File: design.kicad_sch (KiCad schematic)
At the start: 28 parts, among them J2 SKEDD:490107670612, U1 MCP1700x-330xxTT, U2 TCK108AF,LF, U3 ESP32-C3-WROOM-02-N4, U4 TTP223

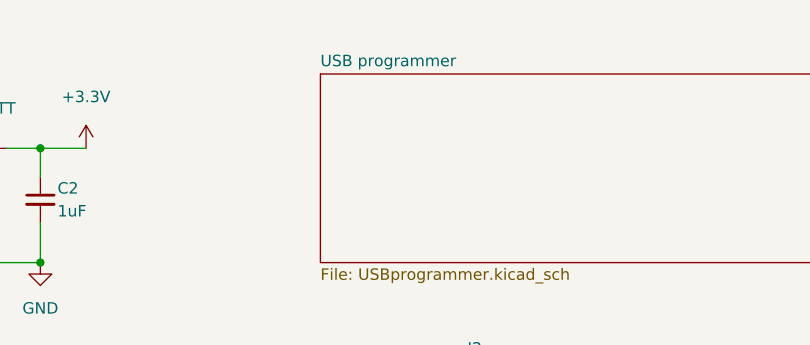
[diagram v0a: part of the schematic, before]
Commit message: remove " " in name
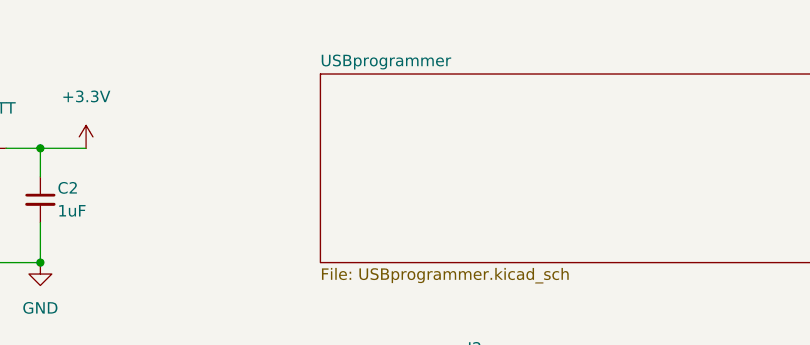
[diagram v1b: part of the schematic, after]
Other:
- sheet USB programmer renamed USBprogrammer
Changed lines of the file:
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@@
     (stroke (width 0.1524) (type solid) (color 0 0 0 0))
     (fill (color 0 0 0 0.0000))
-    (property "Sheet name" "USB programmer" (id 0) (at 207.645 20.8784 0)
+    (property "Sheet name" "USBprogrammer" (id 0) (at 207.645 20.8784 0)
       (effects (font (size 1.27 1.27)) (justify left bottom))
     )

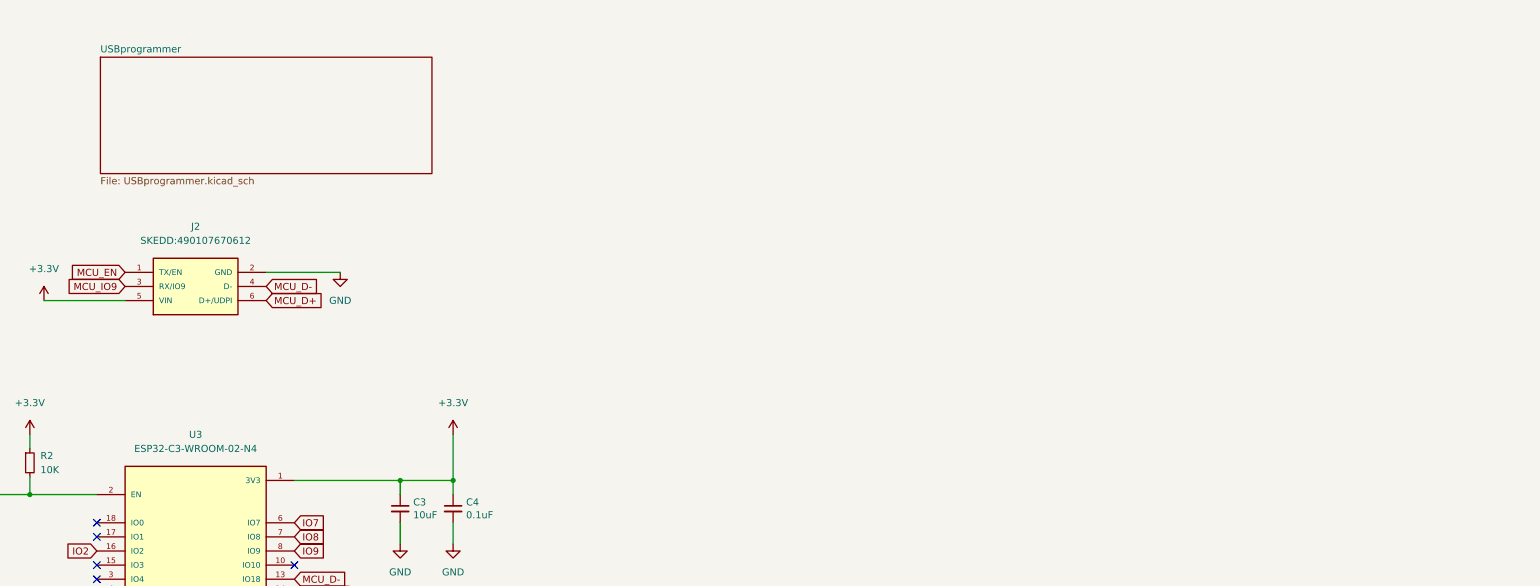
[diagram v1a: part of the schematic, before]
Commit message: revert subsheet in SCH
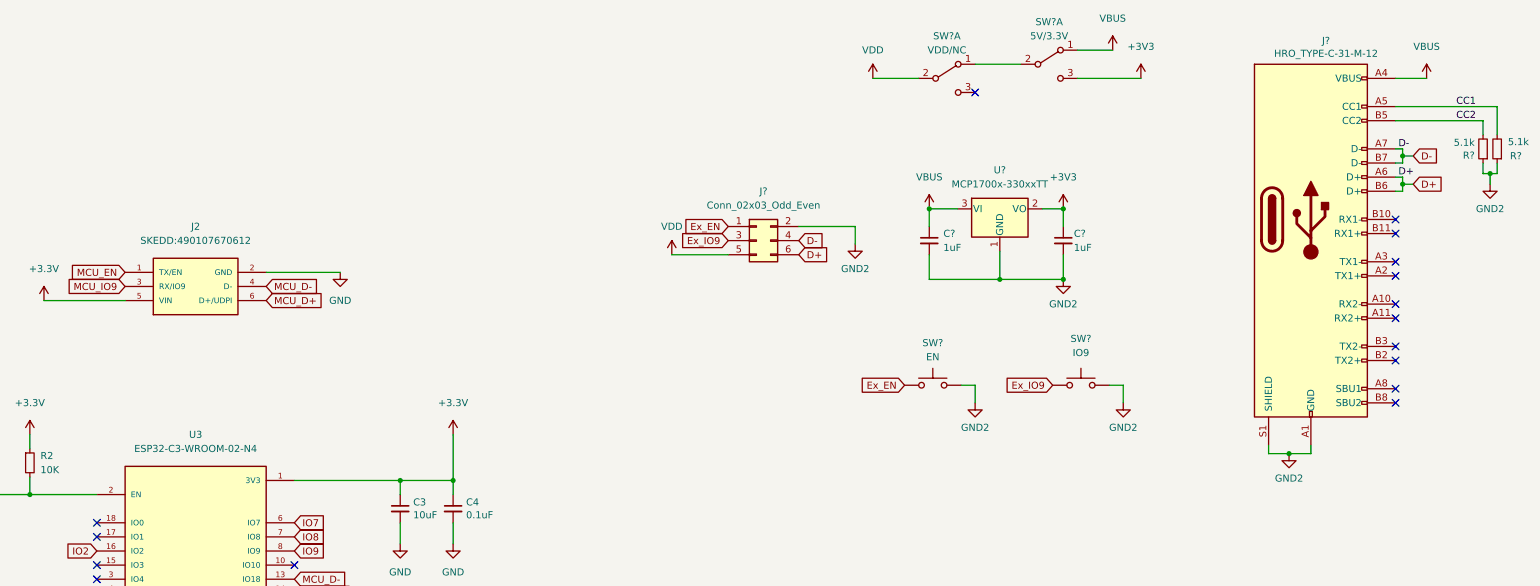
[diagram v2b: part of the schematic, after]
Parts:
- added C? (x2): 1uF, Capacitor_SMD:C_0805_2012Metric, symbol Device:C_Small
- added J?: Conn_02x03_Odd_Even, Connector_PinHeader_2.54mm:PinHeader_2x03_P2.54mm_Vertical, symbol Connector_Generic:Conn_02x03_Odd_Even
- added J?: HRO_TYPE-C-31-M-12, Connector_USB:USB_C_Receptacle_HRO_TYPE-C-31-M-12, symbol Connector:USB_C_Receptacle
- added R? (x2): 5.1k, Resistor_SMD:R_0805_2012Metric, symbol Device:R_Small
- added SW?: EN, Button_Switch_SMD_custom:RKB2, symbol Switch:SW_Push
- added SW?: IO9, Button_Switch_SMD_custom:RKB2, symbol Switch:SW_Push
- added SW?: VDD/NC, Button_Switch_SMD:SW_DPDT_CK_JS202011JCQN, symbol Switch:SW_DPDT_x2
- added SW?: 5V/3.3V, Button_Switch_SMD:SW_DPDT_CK_JS202011JCQN, symbol Switch:SW_DPDT_x2
- added U?: MCP1700x-330xxTT, Package_TO_SOT_SMD:SOT-23, symbol Regulator_Linear:MCP1700x-330xxTT
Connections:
- new net: SW?.1 (A), SW?.2 (B)
- new net +3V3: C?.1, SW?.3 (C), U?.2 (VO)
- new net CC1: J?.A5 (CC1), R?.2
- new net CC2: J?.B5 (CC2), R?.2
- new net D+: J?.6 (Pin_6), J?.A6 (D+), J?.B6 (D+)
- new net D-: J?.4 (Pin_4), J?.A7 (D-), J?.B7 (D-)
- new net Ex_EN: J?.1 (Pin_1), SW?.1
- new net Ex_IO9: J?.3 (Pin_3), SW?.1
- new net GND2: C?.2, C?.2, J?.2 (Pin_2), J?.A1 (GND), J?.A12 (GND), J?.B1 (GND), J?.B12 (GND), J?.S1 (SHIELD), R?.1, R?.1, SW?.2, SW?.2, U?.1 (GND)
- new net VBUS: C?.1, J?.A4 (VBUS), J?.A9 (VBUS), J?.B4 (VBUS), J?.B9 (VBUS), SW?.1 (A), U?.3 (VI)
- new net VDD: J?.5 (Pin_5), SW?.2 (B)
- no-connect marks 8 -> 19
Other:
- removed sheet USBprogrammer
